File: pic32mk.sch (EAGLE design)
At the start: 93 parts, among them IC1 PIC32MK1024MCF100-I_PT, IC10 5.0VDC, IC11 3.3VDC, IC2 ADM3095EBRZ, IC3 TXB0101DCKR, IC4 MAX203ECWP, IC5 TXB0101DCKR, IC6 TXB0101DCKR, IC7 TXB0101DCKR, IC8 TXB0101DCKR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

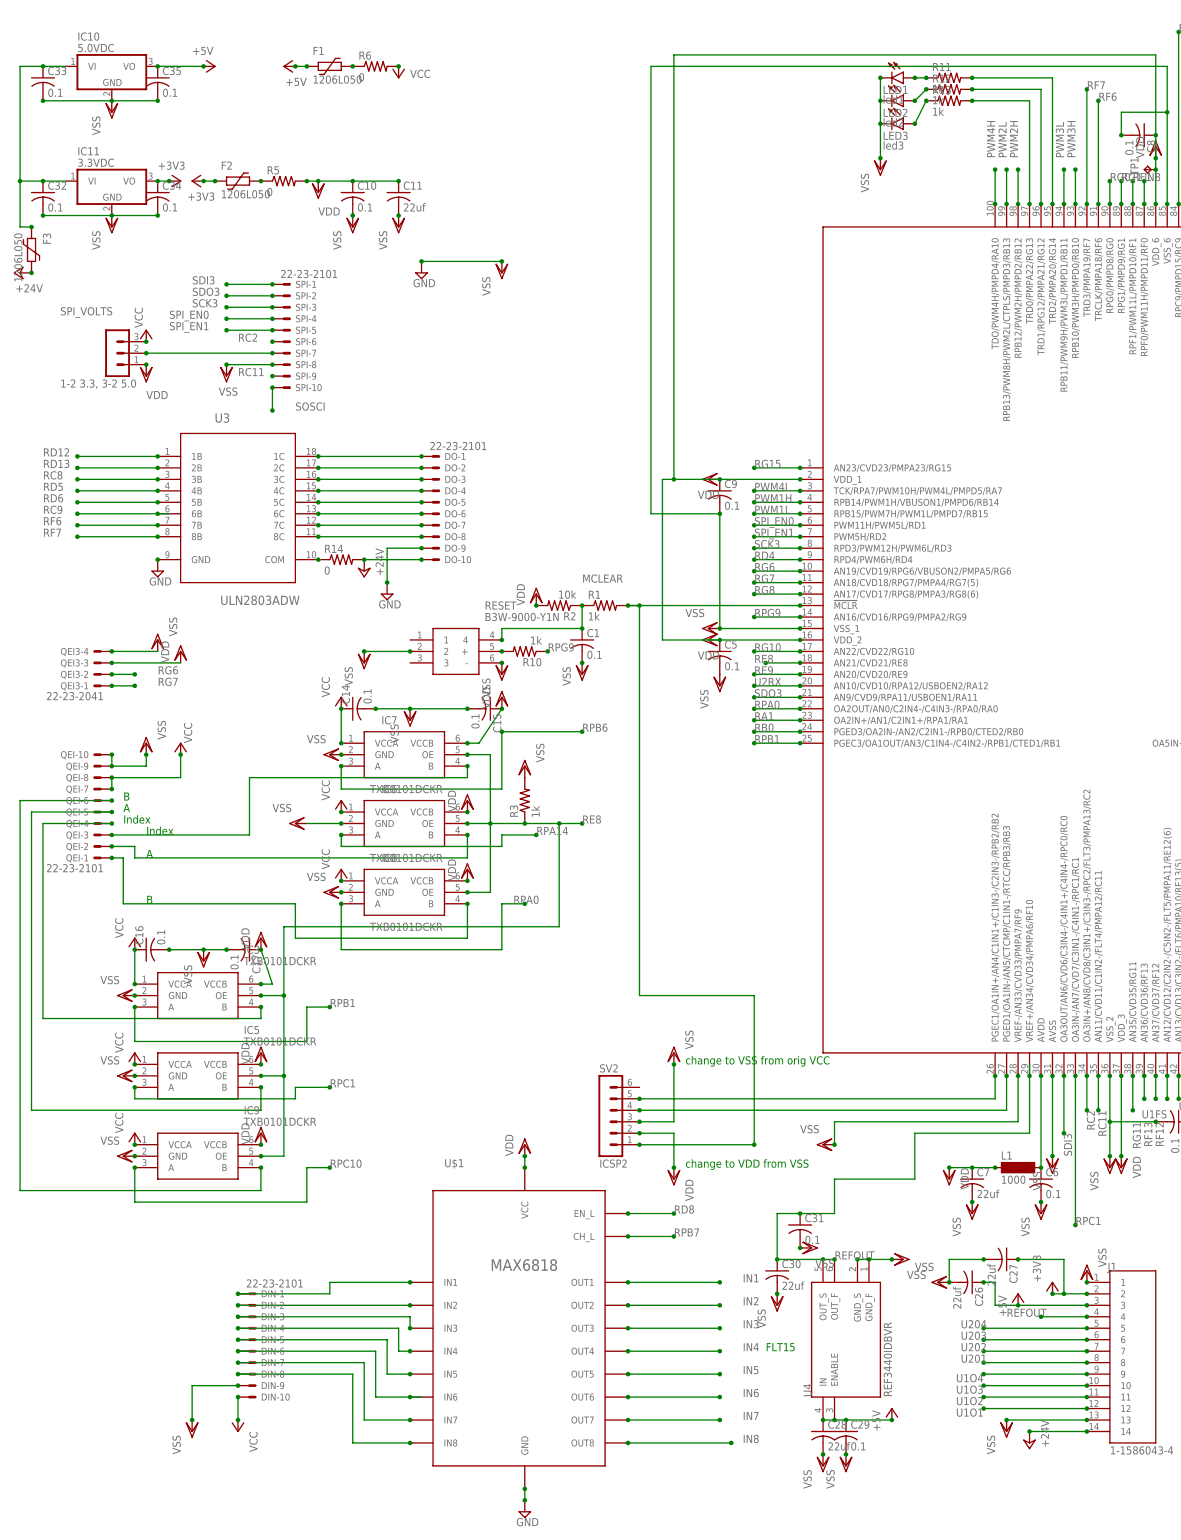
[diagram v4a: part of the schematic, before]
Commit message: add bulk caps
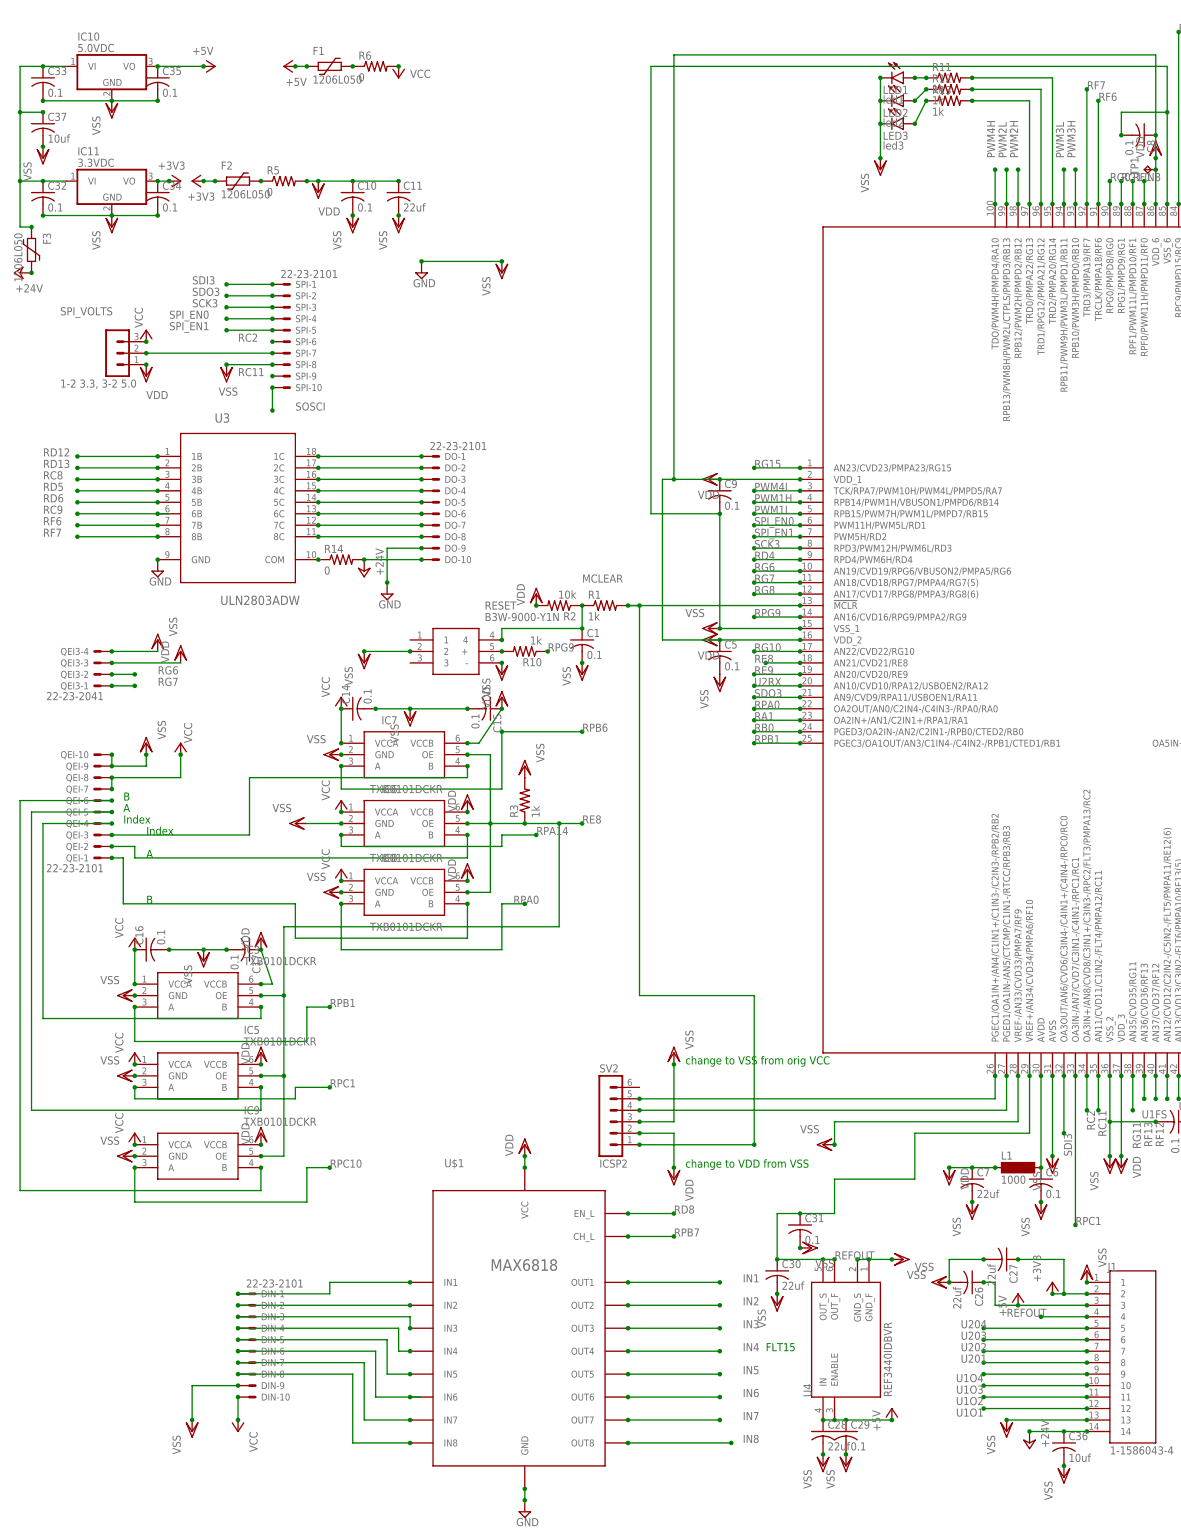
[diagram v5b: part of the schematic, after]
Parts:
- added C36, C37: 10uf, rcl:C-USC1206
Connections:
- net +24V: now also C36.1
- net N$30: now also C37.1
- net VSS: now also C36.2, C37.2
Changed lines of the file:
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@@
 <part name="VSS71" library="supply1" library_urn="urn:adsk.eagle:library:371" deviceset="VSS" device=""/>
 <part name="VDD27" library="supply1" library_urn="urn:adsk.eagle:library:371" deviceset="VDD" device=""/>
+<part name="C36" library="rcl" library_urn="urn:adsk.eagle:library:334" deviceset="C-US" device="C1206" package3d_urn="urn:adsk.eagle:package:23618/2" value="10uf"/>
+<part name="VSS72" library="supply1" library_urn="urn:adsk.eagle:library:371" deviceset="VSS" device=""/>
+<part name="C37" library="rcl" library_urn="urn:adsk.eagle:library:334" deviceset="C-US" device="C1206" package3d_urn="urn:adsk.eagle:package:23618/2" value="10uf"/>
+<part name="VSS73" library="supply1" library_urn="urn:adsk.eagle:library:371" deviceset="VSS" device=""/>
 </parts>
 <sheets>
@@
 <attribute name="VALUE" x="-127" y="2.54" size="1.778" layer="96" rot="R90"/>
 </instance>
+<instance part="C36" gate="G$1" x="71.12" y="-170.18" smashed="yes">
+<attribute name="NAME" x="72.136" y="-169.545" size="1.778" layer="95"/>
+<attribute name="VALUE" x="72.136" y="-174.371" size="1.778" layer="96"/>
+</instance>
+<instance part="VSS72" gate="G$1" x="71.12" y="-177.8" smashed="yes">
+<attribute name="VALUE" x="68.58" y="-182.88" size="1.778" layer="96" rot="R90"/>
+</instance>
+<instance part="C37" gate="G$1" x="-154.94" y="121.92" smashed="yes">
+<attribute name="NAME" x="-153.924" y="122.555" size="1.778" layer="95"/>
+<attribute name="VALUE" x="-153.924" y="117.729" size="1.778" layer="96"/>
+</instance>
+<instance part="VSS73" gate="G$1" x="-154.94" y="114.3" smashed="yes">
+<attribute name="VALUE" x="-157.48" y="109.22" size="1.778" layer="96" rot="R90"/>
+</instance>
 </instances>
 <busses>
@@
 <pinref part="VSS71" gate="G$1" pin="VSS"/>
 </segment>
+<segment>
+<pinref part="C36" gate="G$1" pin="2"/>
+<pinref part="VSS72" gate="G$1" pin="VSS"/>
+<junction x="71.12" y="-175.26"/>
+</segment>
+<segment>
+<pinref part="C37" gate="G$1" pin="2"/>
+<pinref part="VSS73" gate="G$1" pin="VSS"/>
+<junction x="-154.94" y="116.84"/>
+</segment>
 </net>
 <net name="+5V" class="1">
@@
 <segment>
 <pinref part="J1" gate="G$1" pin="14"/>
-<wire x1="76.2" y1="-167.64" x2="63.5" y2="-167.64" width="0.1524" layer="91"/>
+<wire x1="76.2" y1="-167.64" x2="71.12" y2="-167.64" width="0.1524" layer="91"/>
 <pinref part="P+13" gate="1" pin="+24V"/>
 <junction x="63.5" y="-167.64"/>
 <junction x="76.2" y="-167.64"/>
+<pinref part="C36" gate="G$1" pin="1"/>
+<wire x1="71.12" y1="-167.64" x2="63.5" y2="-167.64" width="0.1524" layer="91"/>
+<junction x="71.12" y="-167.64"/>
 </segment>
 <segment>
@@
 <wire x1="-157.48" y1="99.06" x2="-160.02" y2="99.06" width="0.1524" layer="91"/>
 <wire x1="-160.02" y1="99.06" x2="-160.02" y2="109.22" width="0.1524" layer="91"/>
-<wire x1="-160.02" y1="109.22" x2="-160.02" y2="134.62" width="0.1524" layer="91"/>
+<wire x1="-160.02" y1="109.22" x2="-160.02" y2="124.46" width="0.1524" layer="91"/>
+<wire x1="-160.02" y1="124.46" x2="-160.02" y2="134.62" width="0.1524" layer="91"/>
 <wire x1="-160.02" y1="134.62" x2="-154.94" y2="134.62" width="0.1524" layer="91"/>
 <junction x="-157.48" y="99.06"/>
@@
 <junction x="-154.94" y="109.22"/>
 <junction x="-160.02" y="109.22"/>
+<pinref part="C37" gate="G$1" pin="1"/>
+<wire x1="-154.94" y1="124.46" x2="-160.02" y2="124.46" width="0.1524" layer="91"/>
+<junction x="-154.94" y="124.46"/>
+<junction x="-160.02" y="124.46"/>
 </segment>
 </net>

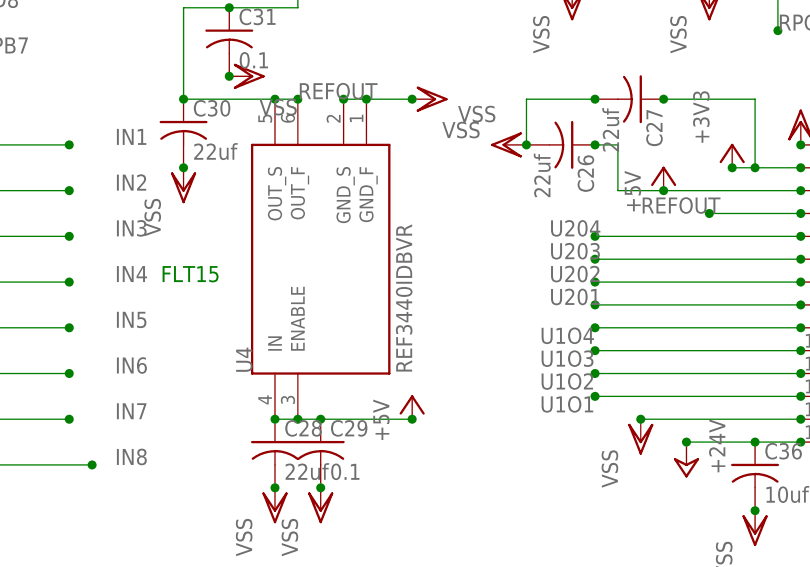
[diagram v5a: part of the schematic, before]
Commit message: add switch code
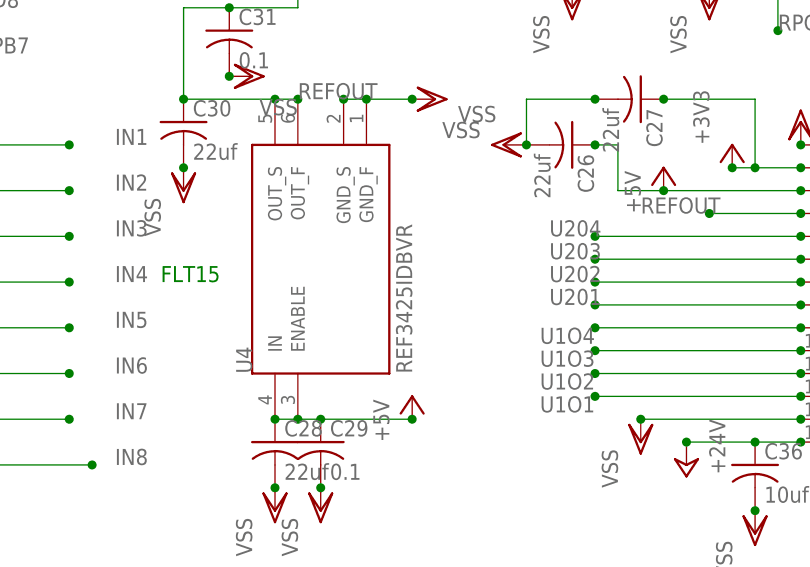
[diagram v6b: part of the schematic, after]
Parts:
- U4: value REF3440IDBVR -> REF3425IDBVR
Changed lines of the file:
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@@
 <part name="P+31" library="supply1" library_urn="urn:adsk.eagle:library:371" deviceset="VCC" device=""/>
 <part name="JP3" library="pinhead" library_urn="urn:adsk.eagle:library:325" deviceset="PINHD-1X16" device="" package3d_urn="urn:adsk.eagle:package:22432/2" value="io pins"/>
-<part name="U4" library="REF3440IDBVR" deviceset="REF3440IDBVR" device=""/>
+<part name="U4" library="REF3440IDBVR" deviceset="REF3440IDBVR" device="" value="REF3425IDBVR"/>
 <part name="VSS61" library="supply1" library_urn="urn:adsk.eagle:library:371" deviceset="VSS" device=""/>
 <part name="P+32" library="supply1" library_urn="urn:adsk.eagle:library:371" deviceset="+5V" device=""/>
